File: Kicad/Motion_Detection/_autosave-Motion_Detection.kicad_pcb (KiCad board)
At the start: 2 copper layers, 65 x 75 mm, 41 parts, among them J1 12V input, J2 SE-10, J3 SEN0192_MW, J4 EKMB, J5 3V3 Output, J6 ZRE200GE, J7 5V Ext, J8 3V3 EN, J9 3V3 Output, P1 XBee, U1 LM7805_TO220, U2 LM324

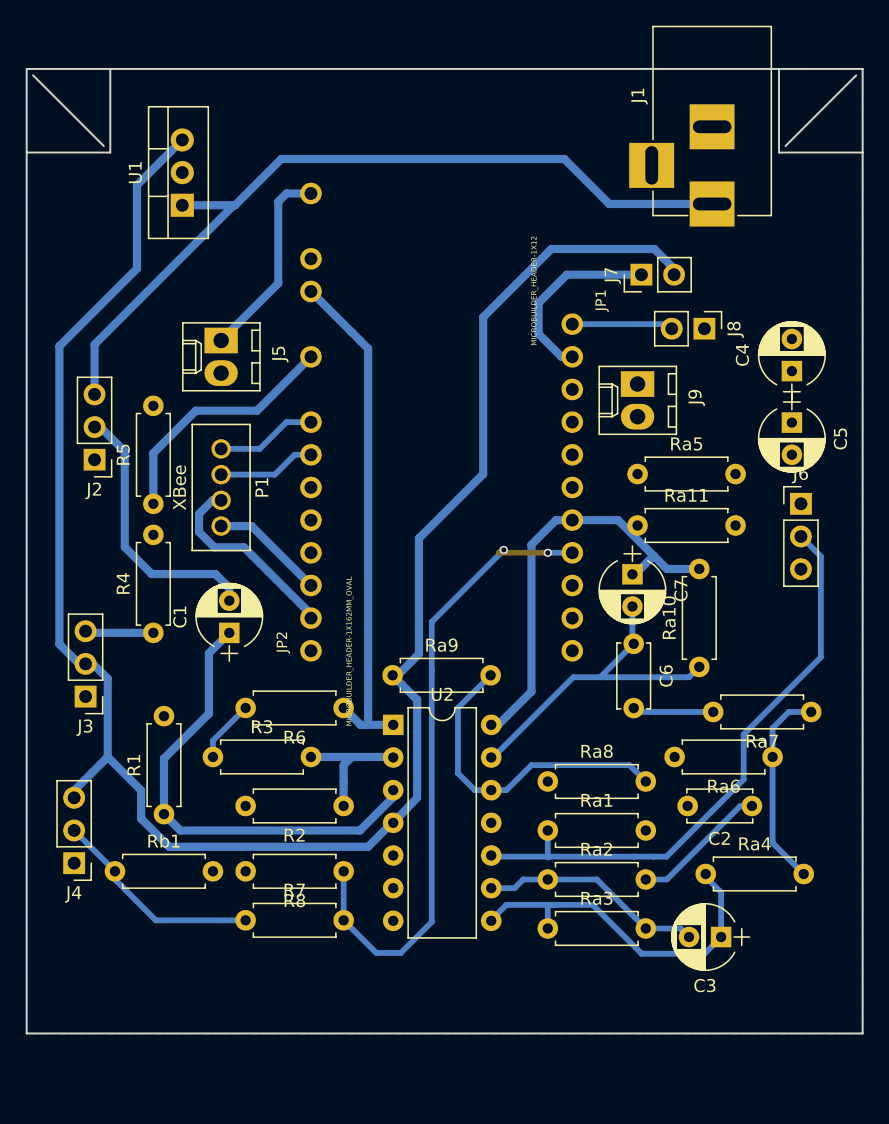
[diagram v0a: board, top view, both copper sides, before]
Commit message: Status led pin added to schematic and PCB.
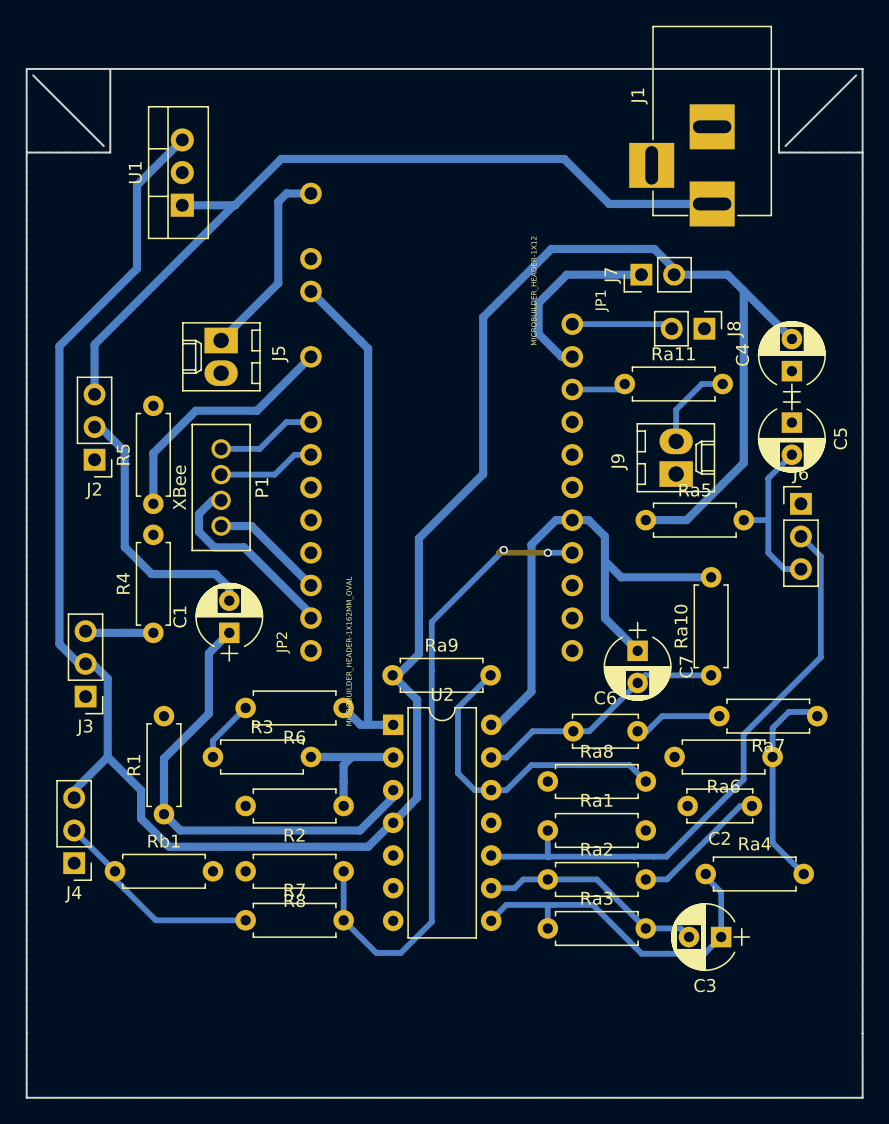
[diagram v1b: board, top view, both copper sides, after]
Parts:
- moved Ra11 11.0 mm to (166.0, 98.0)
- moved C6 8.27 mm to (162.0, 125.0), turned to 0 degrees
- moved J9 7.62 mm to (170.0, 105.0), turned to 90 degrees
- moved C7 5.96 mm to (167.0, 118.7)
- moved Ra5 3.64 mm to (167.6, 108.6)
- moved Ra10 1.13 mm to (172.7, 120.7)
- moved Ra7 0.58 mm to (181.0, 123.8)
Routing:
- net 5V: track 147.8 -> 181.9 mm
- net Net-(C5-Pad2): track 0.00 -> 13.9 mm
- net ZRE200_OUT_: track 33.3 -> 41.4 mm
- net Net-(J9-Pad2): track 0.00 -> 6.91 mm
- net Net-(C6-Pad1): track 26.5 -> 20.8 mm
- net ACTIVITY_LED: track 0.00 -> 4.25 mm
- net Net-(C6-Pad2): track 6.30 -> 6.84 mm
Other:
- board size 65 x 75 mm -> 65 x 80 mm
